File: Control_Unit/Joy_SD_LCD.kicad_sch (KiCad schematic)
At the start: 15 parts, among them SW2 JS5208

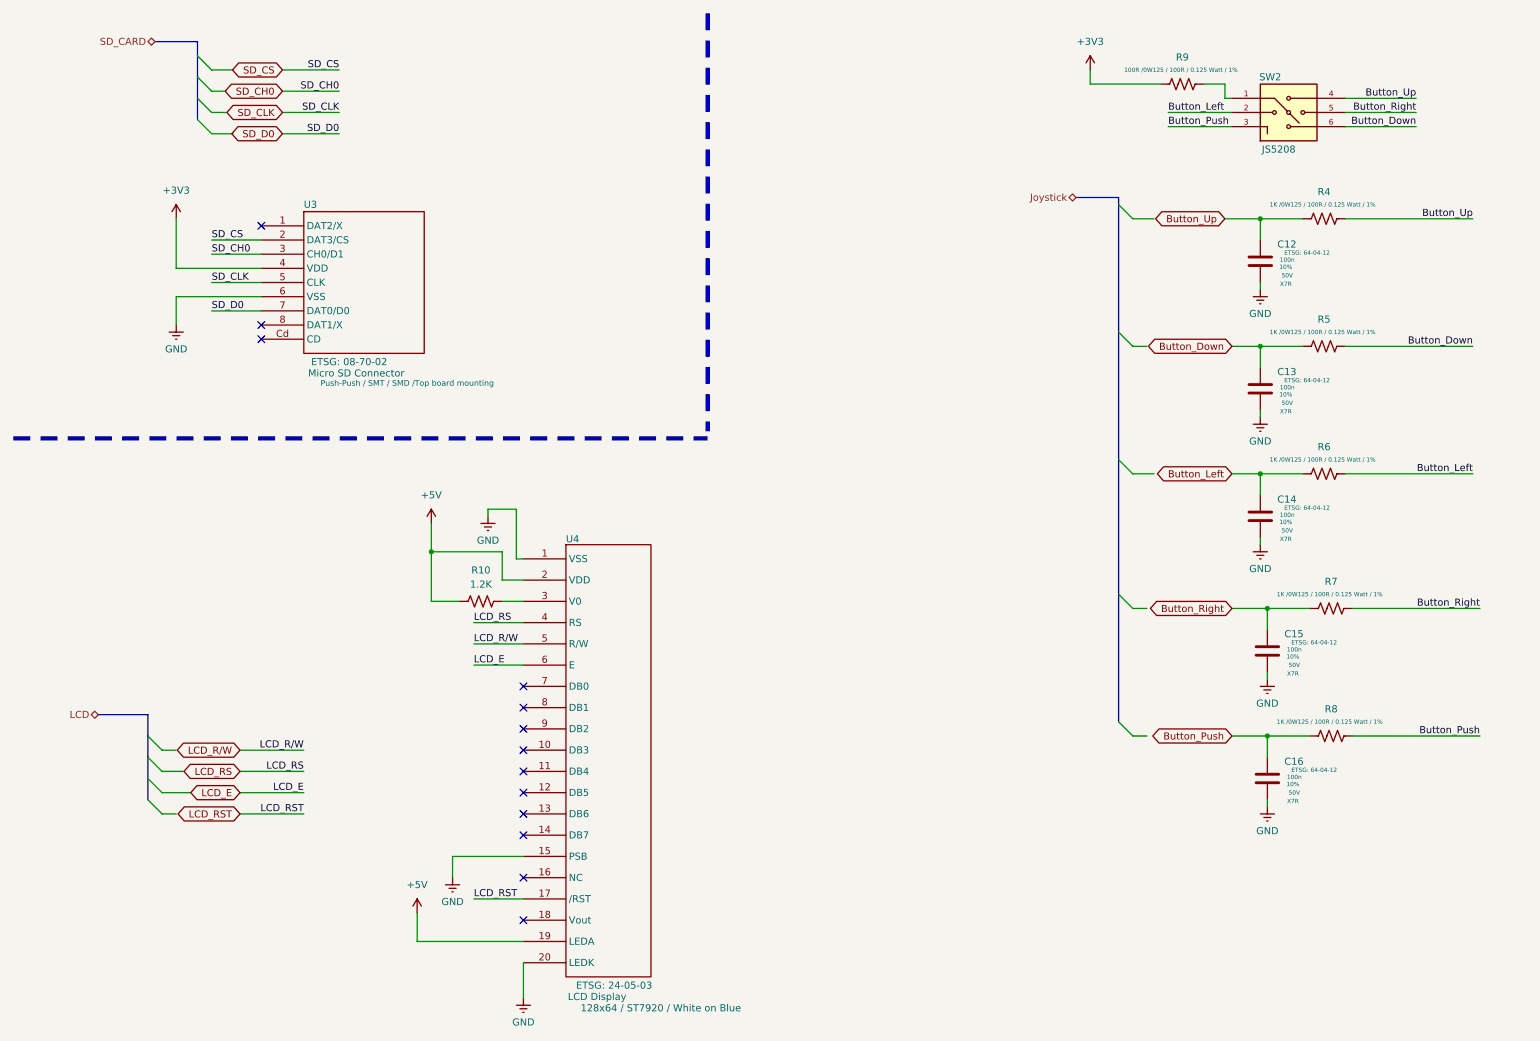
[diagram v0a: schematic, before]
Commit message: Control Unit Schematics and PCB.
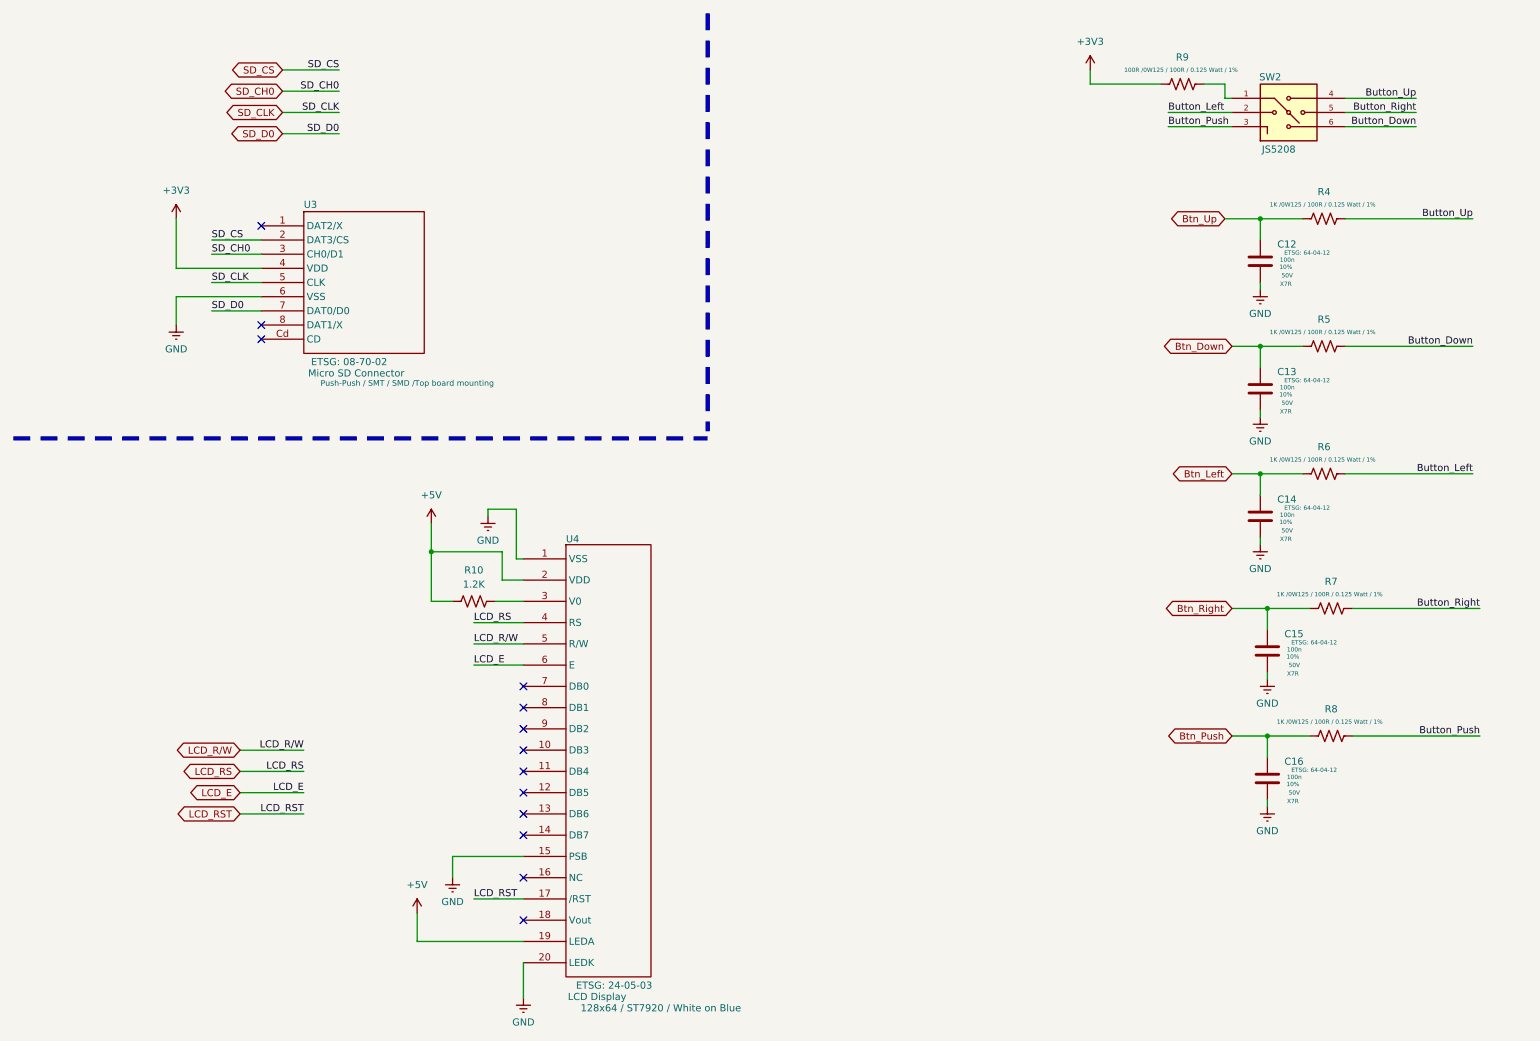
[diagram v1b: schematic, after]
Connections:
- net Button_Down: no longer C13.1, R5.2
- net Button_Left: no longer C14.1, R6.2
- net Button_Push: no longer C16.1, R8.2
- net Button_Right: no longer C15.1, R7.2
- net Button_Up: no longer C12.1, R4.2
- new net Btn_Down: C13.1, R5.2
- new net Btn_Left: C14.1, R6.2
- new net Btn_Push: C16.1, R8.2
- new net Btn_Right: C15.1, R7.2
- new net Btn_Up: C12.1, R4.2
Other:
- moved on the sheet: R10

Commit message: Final Control Unit Schematic Rev 1.
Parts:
- R10: value 1.2K -> 1K2/ 1%/ 0W125; Field5 (none) -> ETSG: 02-69-02
- R4, R5, R6, R7, R8: value 1K /0W125 / 100R / 0.125 Watt / 1% -> 100R/ 1%/ 0W125
- R9: value 100R /0W125 / 100R / 0.125 Watt / 1% -> 100R/ 1%/ 0W125
- renumbered U4 to P2
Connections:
- net Button_Down is gone; now on net BTN_DOWN: R5.1, SW2.6
- net Button_Left is gone; now on net BTN_LEFT: R6.1, SW2.2
- net Button_Push is gone; now on net BTN_PUSH: R8.1, SW2.3
- net Button_Right is gone; now on net BTN_RIGHT: R7.1, SW2.5
- net Button_Up is gone; now on net BTN_UP: R4.1, SW2.4
- net Btn_Down renamed BTN_DOWN
- net Btn_Left renamed BTN_LEFT
- net Btn_Push renamed BTN_PUSH
- net Btn_Right renamed BTN_RIGHT
- net Btn_Up renamed BTN_UP
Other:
- note added: "Joystick"
- note added: "LCD"
- note added: "Micro SD"
- title: (none) -> ENGG3800 Team 03: Loggy
- moved on the sheet: C12, C13, C14, C15, C16, P2, R10, R4, R5, R6, R7, R8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
